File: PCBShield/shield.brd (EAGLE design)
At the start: 160 x 100 mm, 69 parts

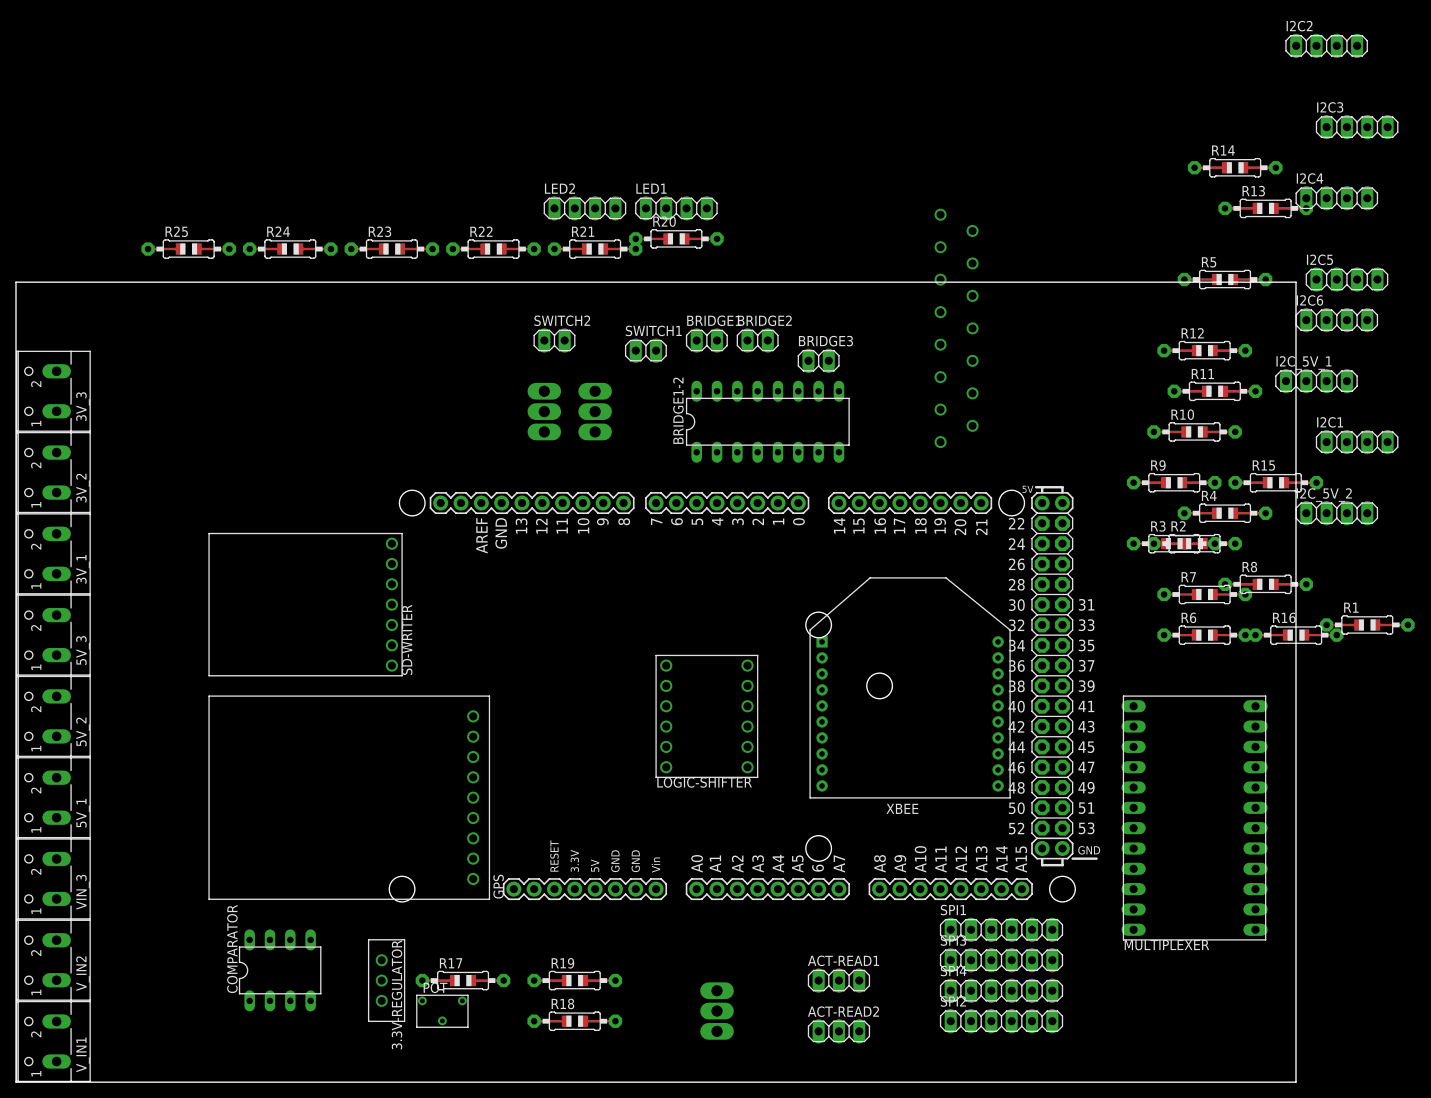
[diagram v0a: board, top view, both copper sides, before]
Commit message: Board is laid out and ready for routing. Screw terminals replace
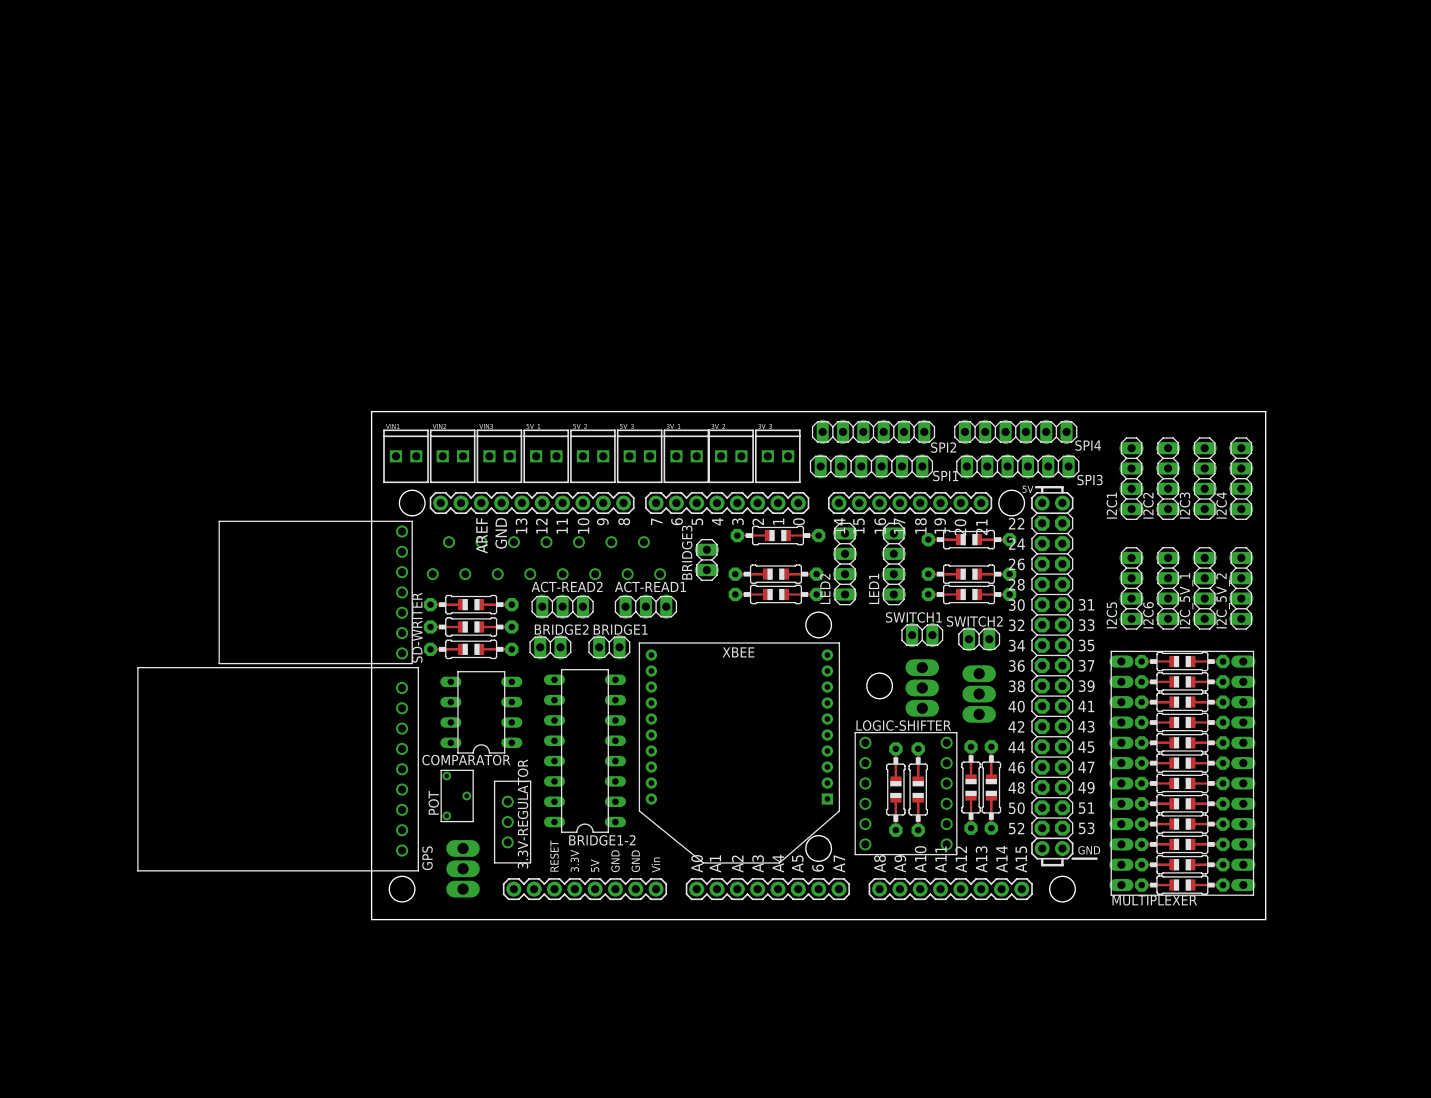
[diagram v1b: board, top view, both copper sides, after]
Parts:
- removed VIN_3, V_IN1, V_IN2: (no value), con-wago-500:W237-102
- added VIN1, VIN2, VIN3: (no value), SparkFun-Connectors:1X02_2.54_SCREWTERM
- 3V_1, 3V_2, 3V_3, 5V_1, 5V_2, 5V_3: device con-wago-500:W237-102 -> SparkFun-Connectors:1X02_2.54_SCREWTERM
- moved 3V_3 90.5 mm to (94.0, 78.2), turned to 0 degrees
- moved 3V_2 84.4 mm to (88.1, 78.2), turned to 0 degrees
- moved R25 81.9 mm to (95.2, 68.3)
- moved 3V_1 79.7 mm to (82.5, 78.2), turned to 0 degrees
- moved 5V_3 76.2 mm to (76.7, 78.2), turned to 0 degrees
- moved SPI2 75.4 mm to (107.2, 81.3), turned to 180 degrees
- moved 5V_1 74.6 mm to (65.0, 78.2), turned to 0 degrees
- moved 5V_2 74.5 mm to (70.9, 78.2), turned to 0 degrees
- moved R24 73.1 mm to (95.0, 63.5)
- moved SPI4 69.9 mm to (125.0, 81.3), turned to 180 degrees
- moved R22 69.7 mm to (119.1, 67.8), turned to 180 degrees
- moved R5 68.3 mm to (145.8, 32.3), turned to 180 degrees
- moved R14 67.1 mm to (145.8, 47.5), turned to 180 degrees
- moved R12 65.5 mm to (112.8, 36.6), turned to 90 degrees
- moved R13 65.1 mm to (145.8, 45.0), turned to 180 degrees
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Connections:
- net N$18 renamed POWER-ON
- net +3V3: no longer 3V_1.1, 3V_2.1, 3V_3.1
- net +5V: no longer 5V_1.1, 5V_2.1, 5V_3.1
- net GND: now also 3V_1.P1, 3V_2.P1, 3V_3.P1, 5V_1.P1, 5V_2.P1, 5V_3.P1, PCB2.GND..., VIN1.P1, VIN2.P1, VIN3.P1; no longer 3V_1.2, 3V_2.2, 3V_3.2, 5V_1.2, 5V_2.2, 5V_3.2, VIN_3.2, V_IN1.2, V_IN2.2
- net SCL3V_5: now also MULTIPLEXER.SCL4; no longer MULTIPLEXER.SDA4
- net SDA3V_5: now also MULTIPLEXER.SDA4; no longer MULTIPLEXER.SCL4
- net SWITCH1_IN: now also SWITCH1-FET.G
- net SWITCH1_LOW: now also SWITCH1-FET.D
- net VCC: no longer VIN_3.1, V_IN1.1, V_IN2.1
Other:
- board size 160 x 100 mm -> 111.8 x 63.5 mm

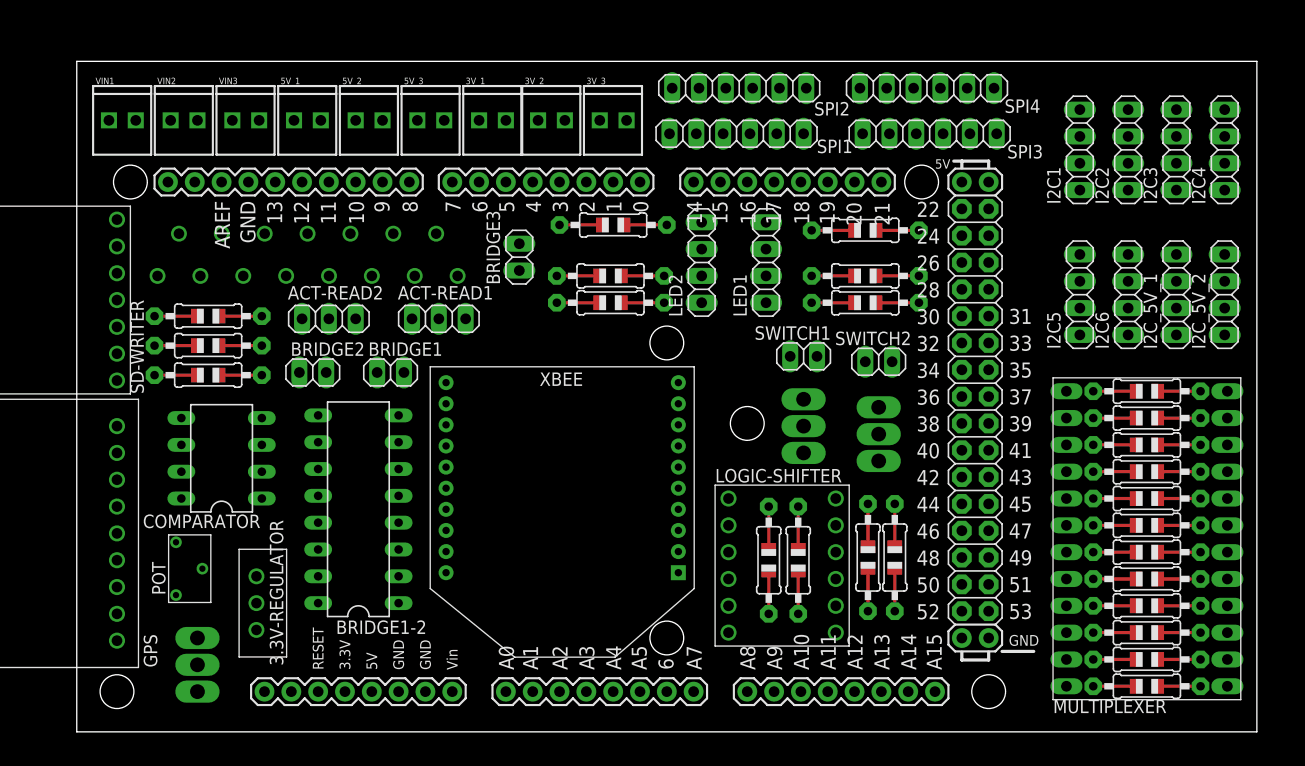
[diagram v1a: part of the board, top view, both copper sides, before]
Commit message: First version of board complete including routing, pending verification
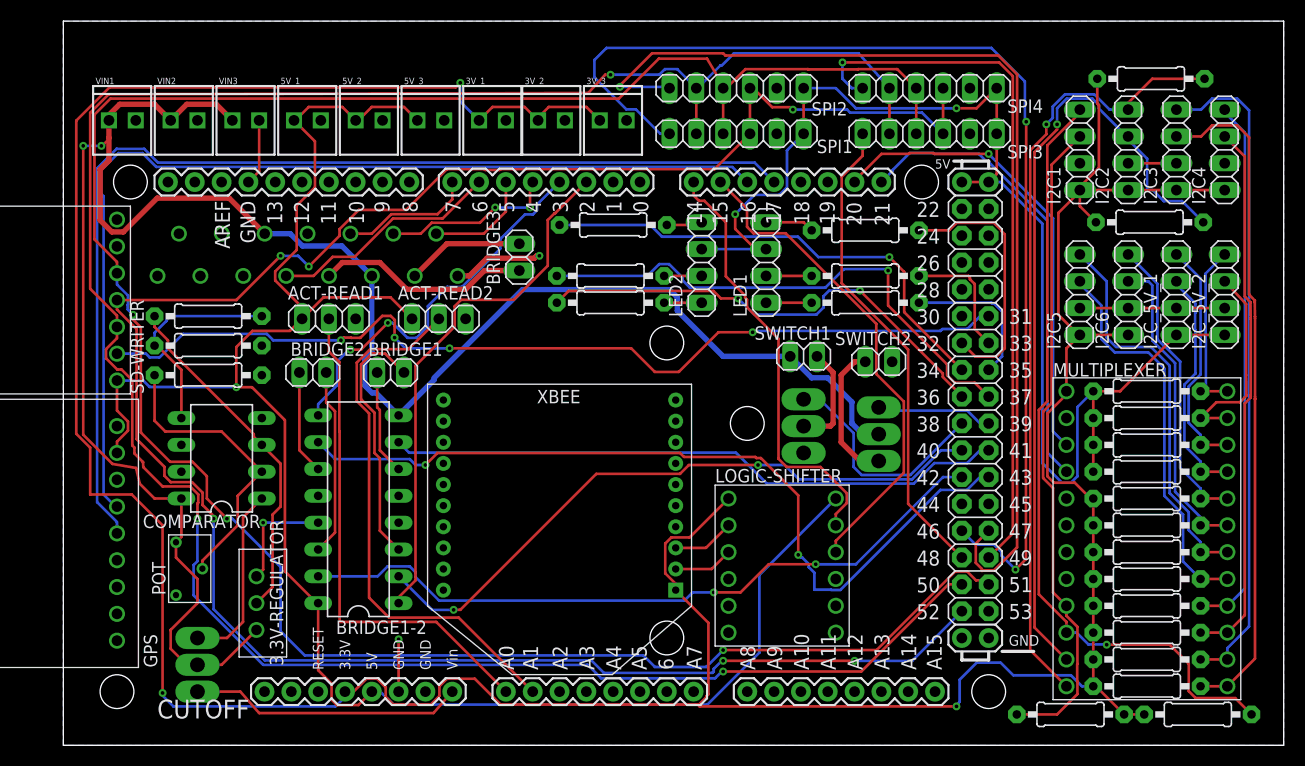
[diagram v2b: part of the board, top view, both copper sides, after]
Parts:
- moved R12 56.5 mm to (146.2, 82.2), turned to 180 degrees
- moved R11 48.2 mm to (146.1, 68.6), turned to 180 degrees
- moved R10 32.3 mm to (150.6, 22.0), turned to 180 degrees
- moved R9 24.3 mm to (138.6, 22.0), turned to 0 degrees
- moved ACT-READ1 10.4 mm to (68.3, 59.4)
- moved ACT-READ2 10.4 mm to (78.7, 59.4)
- moved XBEE 1.67 mm to (90.2, 39.2)
- moved SPI2 0.25 mm to (106.9, 81.3)
- moved SPI4 0.25 mm to (125.2, 81.3)
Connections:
- net N$16 renamed 0.3V
- net +3V3: now also 3V_1.P2, 3V_2.P2, 3V_3.P2
- net +5V: now also 5V_1.P2, 5V_2.P2, 5V_3.P2, PCB2.5V., PCB2.5V..
- net GND: now also PCB2.GND....
- net LED1B: now also PCB2.33; no longer PCB2.36
- net LED1G: now also PCB2.35; no longer PCB2.34
- net LED2G: now also PCB2.36; no longer PCB2.35
- net LED2R: now also PCB2.34; no longer PCB2.33
- net VCC: now also VIN1.P2, VIN2.P2, VIN3.P2
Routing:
- net +3V3: track 0.00 -> 331.8 mm, vias 0 -> 3
- net +5V: track 0.00 -> 297.8 mm, vias 0 -> 3
- net MOSI: track 0.00 -> 222.4 mm, vias 0 -> 3
- net MISO: track 0.00 -> 222.1 mm, vias 0 -> 3
- net SCK: track 0.00 -> 206.6 mm, vias 0 -> 6
- net VCC: track 0.00 -> 196.9 mm, vias 0 -> 2
- net SS1: track 0.00 -> 107.0 mm, vias 0 -> 2
- net TX_GPS: track 0.00 -> 101.5 mm
- net SS2: track 0.00 -> 98.2 mm, vias 0 -> 1
- net RX_GPS: track 0.00 -> 95.5 mm
- net CS_SD: track 0.00 -> 90.3 mm, vias 0 -> 4
- net BRIDGE2B_IN: track 0.00 -> 79.1 mm, vias 0 -> 2
- net SDA3V_2: track 0.00 -> 75.6 mm, vias 0 -> 1
- net SCL3V_1: track 0.00 -> 74.5 mm, vias 0 -> 1
- net SCL3V_2: track 0.00 -> 74.2 mm, vias 0 -> 1
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- added copper zone on layer 16, net GND
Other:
- board size 111.8 x 63.5 mm -> 115.6 x 68.6 mm

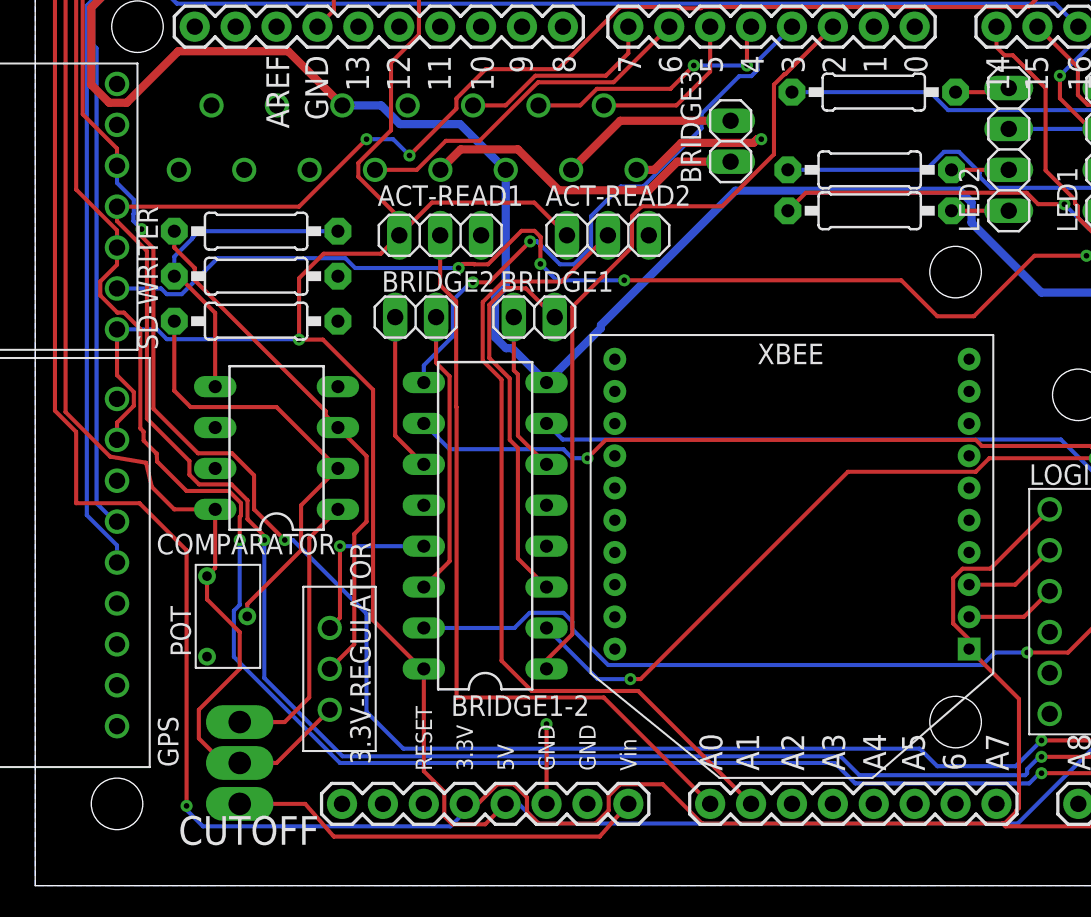
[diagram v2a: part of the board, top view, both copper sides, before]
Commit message: Modified board to fit Xbee Pro size module and completed full BOM
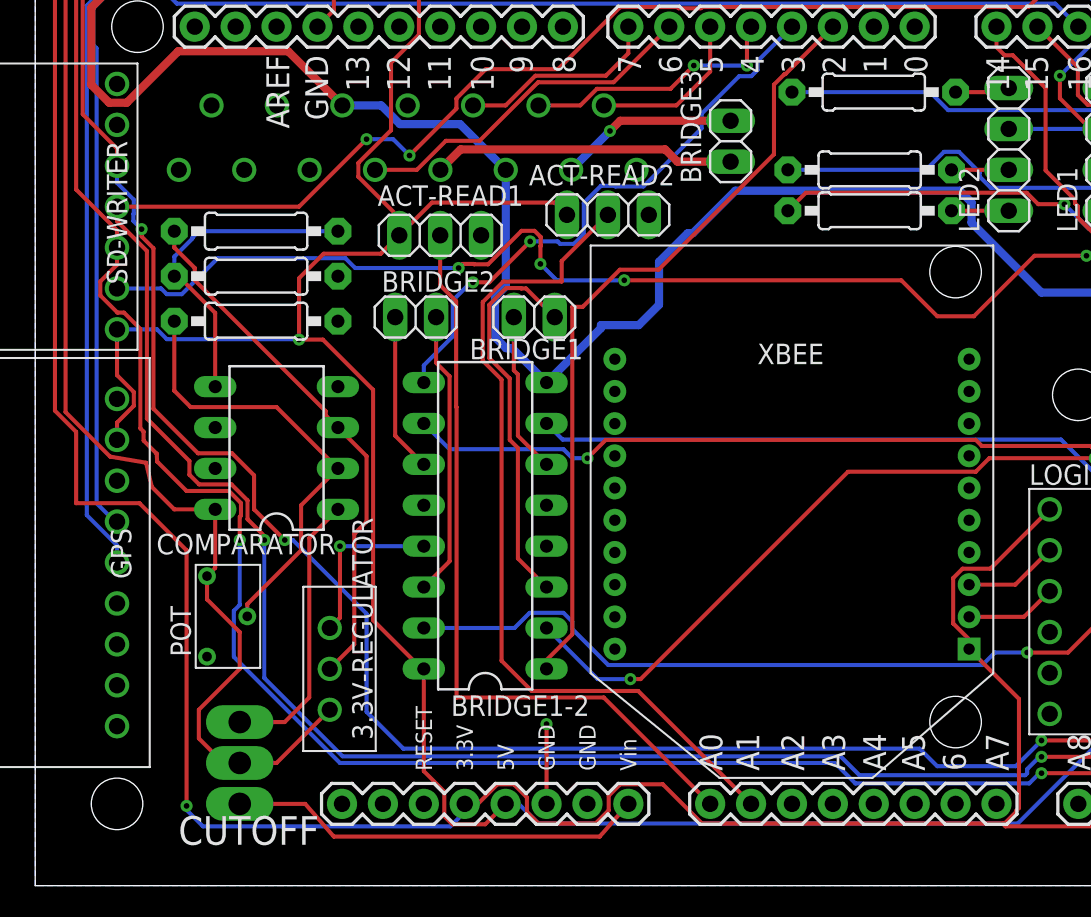
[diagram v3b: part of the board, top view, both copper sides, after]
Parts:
- moved ACT-READ2 1.27 mm to (78.7, 60.7)
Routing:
- net GND: track 48.8 -> 40.2 mm, vias 3 -> 2
- net VCC: track 196.9 -> 198.5 mm
- net BRIDGE3B_OUT: track 20.3 -> 18.9 mm
- net READ_ACT2: track 51.4 -> 52.7 mm
- net BRIDGE1_PWM: track 50.2 -> 49.1 mm
- net BRIDGE2_PWM: track 37.1 -> 36.1 mm
- net +5V: track 297.8 -> 297.2 mm
- net BRIDGE3A_OUT: vias 0 -> 1

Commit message: Final version of PCB for printing
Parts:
- added U$1: 6BOLT, specialparts:6BOLT
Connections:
- net GND: now also U$1.P$1
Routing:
- added copper zone on layer 1, net GND
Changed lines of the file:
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@@
 <element name="3V_2" library="SparkFun-Connectors" library_urn="urn:adsk.eagle:library:513" package="1X02_2.54_SCREWTERM" package3d_urn="urn:adsk.eagle:package:38059/1" value="" x="88.138" y="78.232"/>
 <element name="3V_3" library="SparkFun-Connectors" library_urn="urn:adsk.eagle:library:513" package="1X02_2.54_SCREWTERM" package3d_urn="urn:adsk.eagle:package:38059/1" value="" x="93.98" y="78.232"/>
+<element name="U$1" library="specialparts" package="6BOLT" value="6BOLT" x="137.287" y="83.947"/>
 </elements>
 <signals>
@@
 <via x="74.93" y="29.083" extent="1-16" drill="0.35"/>
 <wire x1="74.93" y1="24.13" x2="74.93" y2="29.083" width="0.254" layer="1"/>
+<contactref element="U$1" pad="P$1"/>
+<polygon width="0.508" layer="1">
+<vertex x="43.18" y="87.63"/>
+<vertex x="158.75" y="87.63"/>
+<vertex x="158.75" y="19.05"/>
+<vertex x="43.307" y="19.05"/>
+<vertex x="43.18" y="19.05"/>
+</polygon>
 </signal>
 <signal name="BRIDGE1_PWM">
